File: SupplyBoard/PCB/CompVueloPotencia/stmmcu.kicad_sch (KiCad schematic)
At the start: 20 parts, among them J2 USB_B_Micro, J3 Conn_01x04, SW2 RESET, SW3 SW_SPDT, U4 STM32F103CBT6, Y1 16Mhz

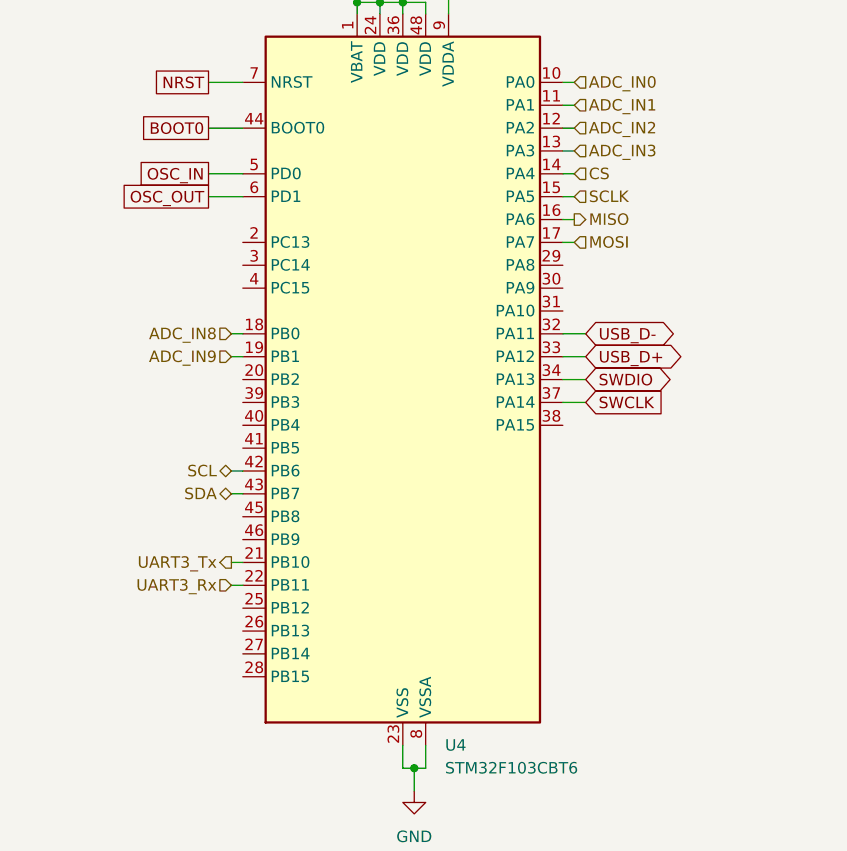
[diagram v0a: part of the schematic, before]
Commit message: Supply board - Update the current measurement
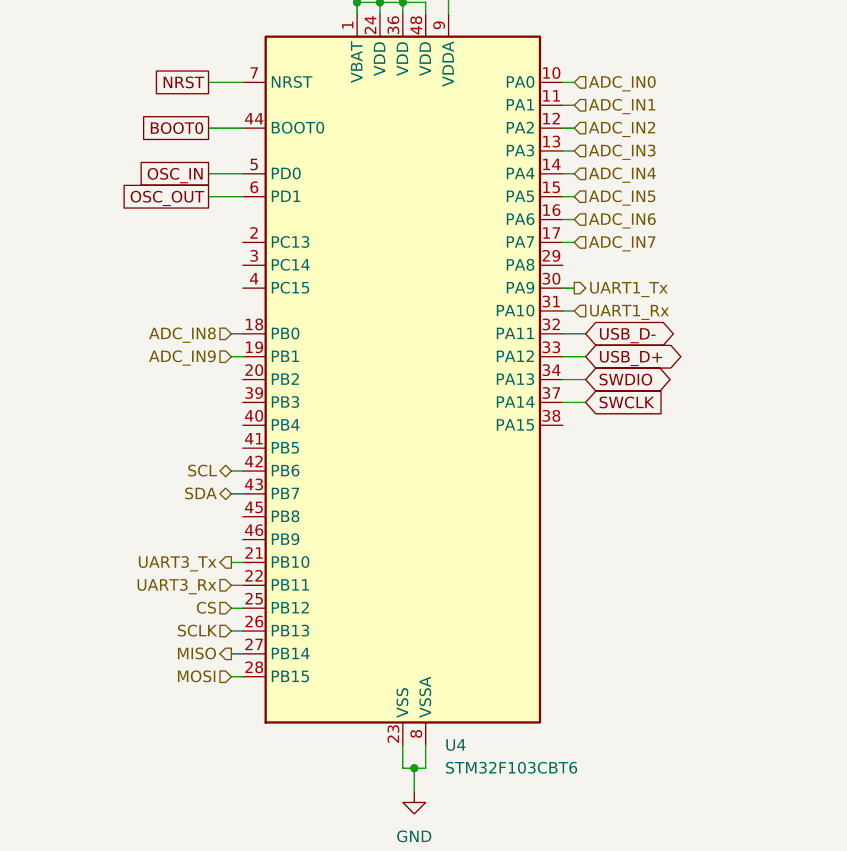
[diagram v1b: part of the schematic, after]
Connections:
- net CS: now also U4.25 (PB12); no longer U4.14 (PA4)
- net MISO: now also U4.27 (PB14); no longer U4.16 (PA6)
- net MOSI: now also U4.28 (PB15); no longer U4.17 (PA7)
- net SCLK: now also U4.26 (PB13); no longer U4.15 (PA5)
- net UART1_Tx: now reaches U4.30 (PA9)
- net UART1_Rx: now reaches U4.31 (PA10)
- new net ADC_IN4: U4.14 (PA4)
- new net ADC_IN5: U4.15 (PA5)
- new net ADC_IN6: U4.16 (PA6)
- new net ADC_IN7: U4.17 (PA7)
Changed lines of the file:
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@@
+	(wire
+		(pts
+			(xy 119.38 124.46) (xy 120.65 124.46)
+		)
+		(stroke
+			(width 0)
+			(type default)
+		)
+	)
 	(wire
 		(pts
@@
 		(pts
 			(xy 31.75 64.77) (xy 35.56 64.77)
+		)
+		(stroke
+			(width 0)
+			(type default)
+		)
+	)
+	(wire
+		(pts
+			(xy 119.38 127) (xy 120.65 127)
 		)
 		(stroke
@@
 	(wire
 		(pts
-			(xy 157.48 76.2) (xy 156.21 76.2)
-		)
-		(stroke
-			(width 0)
-			(type default)
-		)
-	)
-	(wire
-		(pts
 			(xy 138.43 54.61) (xy 135.89 54.61)
 		)
@@
 	(wire
 		(pts
+			(xy 45.72 123.19) (xy 45.72 119.38)
+		)
+		(stroke
+			(width 0)
+			(type default)
+		)
+	)
+	(wire
+		(pts
+			(xy 138.43 139.7) (xy 139.7 139.7)
+		)
+		(stroke
+			(width 0)
+			(type default)
+		)
+	)
+	(wire
+		(pts
+			(xy 233.68 48.26) (xy 233.68 45.72)
+		)
+		(stroke
+			(width 0)
+			(type default)
+		)
+	)
+	(wire
+		(pts
+			(xy 240.03 132.08) (xy 242.57 132.08)
+		)
+		(stroke
+			(width 0)
+			(type default)
+		)
+	)
+	(wire
+		(pts
+			(xy 240.03 129.54) (xy 242.57 129.54)
+		)
+		(stroke
+			(width 0)
+			(type default)
+		)
+	)
+	(wire
+		(pts
+			(xy 240.03 38.1) (xy 246.38 38.1)
+		)
+		(stroke
+			(width 0)
+			(type default)
+		)
+	)
+	(wire
+		(pts
+			(xy 35.56 111.76) (xy 35.56 110.49)
+		)
+		(stroke
+			(width 0)
+			(type default)
+		)
+	)
+	(wire
+		(pts
+			(xy 21.59 168.91) (xy 21.59 171.45)
+		)
+		(stroke
+			(width 0)
+			(type default)
+		)
+	)
+	(wire
+		(pts
+			(xy 157.48 88.9) (xy 156.21 88.9)
+		)
+		(stroke
+			(width 0)
+			(type default)
+		)
+	)
+	(wire
+		(pts
+			(xy 157.48 76.2) (xy 156.21 76.2)
+		)
+		(stroke
+			(width 0)
+			(type default)
+		)
+	)
+	(wire
+		(pts
 			(xy 157.48 81.28) (xy 156.21 81.28)
 		)
@@
 	(wire
 		(pts
-			(xy 45.72 123.19) (xy 45.72 119.38)
-		)
-		(stroke
-			(width 0)
-			(type default)
-		)
-	)
-	(wire
-		(pts
-			(xy 138.43 139.7) (xy 139.7 139.7)
-		)
-		(stroke
-			(width 0)
-			(type default)
-		)
-	)
-	(wire
-		(pts
-			(xy 233.68 48.26) (xy 233.68 45.72)
-		)
-		(stroke
-			(width 0)
-			(type default)
-		)
-	)
-	(wire
-		(pts
-			(xy 240.03 132.08) (xy 242.57 132.08)
-		)
-		(stroke
-			(width 0)
-			(type default)
-		)
-	)
-	(wire
-		(pts
-			(xy 240.03 129.54) (xy 242.57 129.54)
-		)
-		(stroke
-			(width 0)
-			(type default)
-		)
-	)
-	(wire
-		(pts
-			(xy 240.03 38.1) (xy 246.38 38.1)
-		)
-		(stroke
-			(width 0)
-			(type default)
-		)
-	)
-	(wire
-		(pts
-			(xy 35.56 111.76) (xy 35.56 110.49)
-		)
-		(stroke
-			(width 0)
-			(type default)
-		)
-	)
-	(wire
-		(pts
-			(xy 21.59 168.91) (xy 21.59 171.45)
-		)
-		(stroke
-			(width 0)
-			(type default)
-		)
-	)
-	(wire
-		(pts
 			(xy 45.72 115.57) (xy 45.72 119.38)
 		)
@@
 	(wire
 		(pts
+			(xy 157.48 78.74) (xy 156.21 78.74)
+		)
+		(stroke
+			(width 0)
+			(type default)
+		)
+	)
+	(wire
+		(pts
+			(xy 119.38 121.92) (xy 120.65 121.92)
+		)
+		(stroke
+			(width 0)
+			(type default)
+		)
+	)
+	(wire
+		(pts
 			(xy 35.56 110.49) (xy 41.91 110.49)
 		)
@@
 		(pts
 			(xy 133.35 54.61) (xy 133.35 55.88)
+		)
+		(stroke
+			(width 0)
+			(type default)
+		)
+	)
+	(wire
+		(pts
+			(xy 157.48 86.36) (xy 156.21 86.36)
 		)
 		(stroke
@@
 	(wire
 		(pts
+			(xy 157.48 73.66) (xy 156.21 73.66)
+		)
+		(stroke
+			(width 0)
+			(type default)
+		)
+	)
+	(wire
+		(pts
 			(xy 231.14 93.98) (xy 233.68 93.98)
 		)
@@
 	(wire
 		(pts
+			(xy 119.38 129.54) (xy 120.65 129.54)
+		)
+		(stroke
+			(width 0)
+			(type default)
+		)
+	)
+	(wire
+		(pts
 			(xy 119.38 93.98) (xy 120.65 93.98)
 		)
@@
 	(wire
 		(pts
-			(xy 157.48 73.66) (xy 156.21 73.66)
-		)
-		(stroke
-			(width 0)
-			(type default)
-		)
-	)
-	(wire
-		(pts
 			(xy 157.48 71.12) (xy 156.21 71.12)
 		)
@@
 		(pts
 			(xy 49.53 110.49) (xy 54.61 110.49)
-		)
-		(stroke
-			(width 0)
-			(type default)
-		)
-	)
-	(wire
-		(pts
-			(xy 157.48 78.74) (xy 156.21 78.74)
 		)
 		(stroke
@@
 		)
 	)
-	(hierarchical_label "MOSI"
+	(hierarchical_label "CS"
 		(shape input)
-		(at 157.48 81.28 0)
+		(at 119.38 121.92 180)
+		(effects
+			(font
+				(size 1.27 1.27)
+			)
+			(justify right)
+		)
+	)
+	(hierarchical_label "ADC_IN4"
+		(shape input)
+		(at 157.48 73.66 0)
 		(effects
 			(font
@@
 		)
 	)
-	(hierarchical_label "SCLK"
-		(shape input)
-		(at 157.48 76.2 0)
-		(effects
-			(font
-				(size 1.27 1.27)
-			)
-			(justify left)
-		)
-	)
 	(hierarchical_label "UART3_Rx"
 		(shape input)
@@
 		)
 	)
+	(hierarchical_label "UART1_Tx"
+		(shape output)
+		(at 157.48 86.36 0)
+		(effects
+			(font
+				(size 1.27 1.27)
+			)
+			(justify left)
+		)
+	)
 	(hierarchical_label "ADC_IN2"
 		(shape input)
@@
 		)
 	)
+	(hierarchical_label "ADC_IN6"
+		(shape input)
+		(at 157.48 78.74 0)
+		(effects
+			(font
+				(size 1.27 1.27)
+			)
+			(justify left)
+		)
+	)
 	(hierarchical_label "ADC_IN3"
 		(shape input)
@@
 		)
 	)
+	(hierarchical_label "MOSI"
+		(shape input)
+		(at 119.38 129.54 180)
+		(effects
+			(font
+				(size 1.27 1.27)
+			)
+			(justify right)
+		)
+	)
+	(hierarchical_label "MISO"
+		(shape output)
+		(at 119.38 127 180)
+		(effects
+			(font
+				(size 1.27 1.27)
+			)
+			(justify right)
+		)
+	)
 	(hierarchical_label "VDD"
 		(shape input)
@@
 		)
 	)
-	(hierarchical_label "CS"
+	(hierarchical_label "ADC_IN7"
 		(shape input)
-		(at 157.48 73.66 0)
+		(at 157.48 81.28 0)
 		(effects
 			(font
@@
 		)
 	)
-	(hierarchical_label "MISO"
-		(shape output)
-		(at 157.48 78.74 0)
+	(hierarchical_label "ADC_IN5"
+		(shape input)
+		(at 157.48 76.2 0)
 		(effects
 			(font
@@
 		)
 	)
+	(hierarchical_label "SCLK"
+		(shape input)
+		(at 119.38 124.46 180)
+		(effects
+			(font
+				(size 1.27 1.27)
+			)
+			(justify right)
+		)
+	)
 	(hierarchical_label "ADC_IN1"
 		(shape input)
@@
 		)
 	)
+	(hierarchical_label "UART1_Rx"
+		(shape input)
+		(at 157.48 88.9 0)
+		(effects
+			(font
+				(size 1.27 1.27)
+			)
+			(justify left)
+		)
+	)

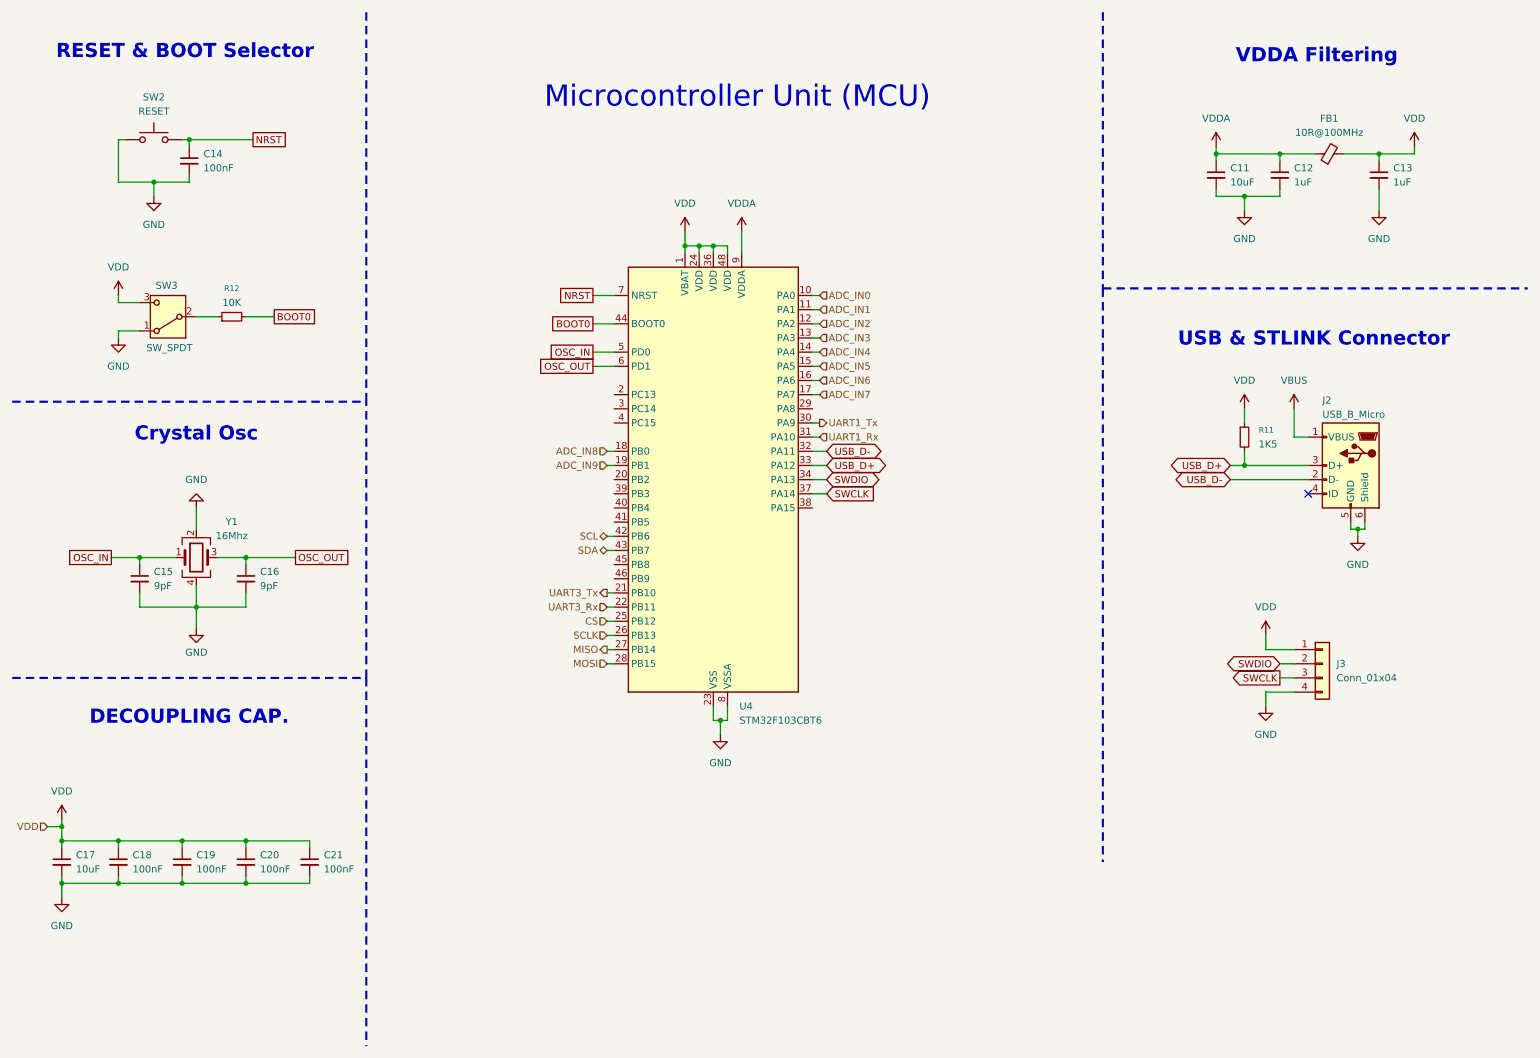
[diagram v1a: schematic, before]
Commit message: SupplyBoard - finish current sense
Finish the Current Sensor Circuit and add more 3.3V out, i change de microcontroles to a mcu that have the exact GPIO's
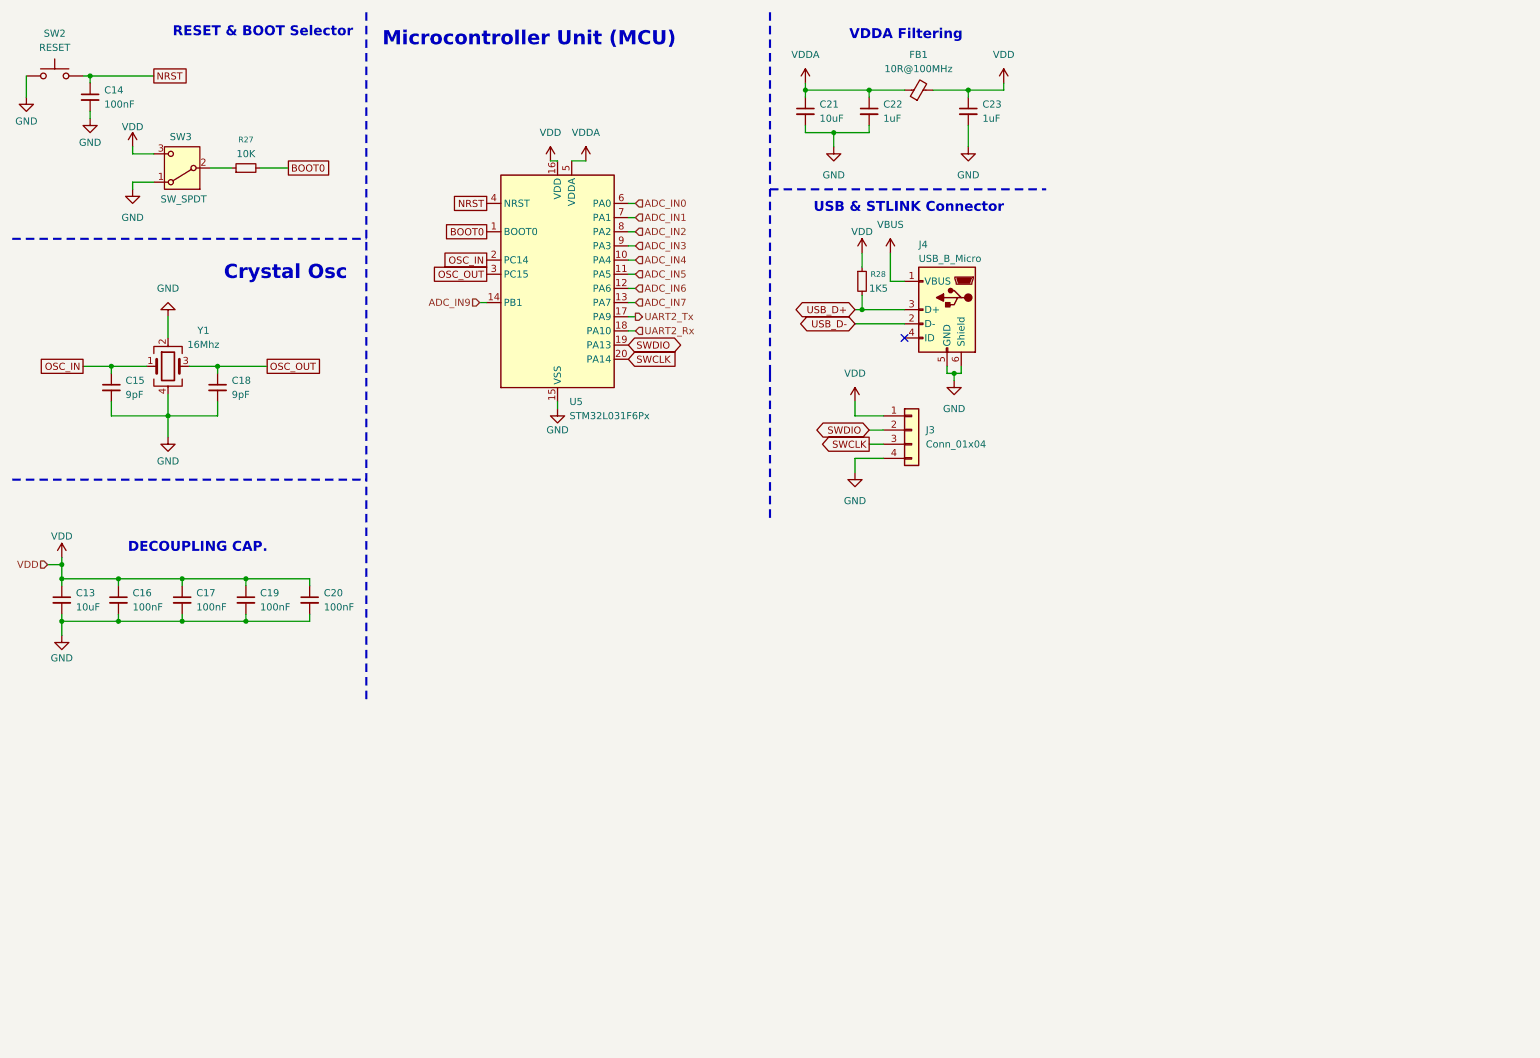
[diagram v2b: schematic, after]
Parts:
- removed U4: STM32F103CBT6, Package_QFP:LQFP-48_7x7mm_P0.5mm, symbol MCU_ST_STM32F1:STM32F103CBTx
- added U5: STM32L031F6Px, Package_SO:TSSOP-20_4.4x6.5mm_P0.65mm, symbol MCU_ST_STM32L0:STM32L031F6Px
- renumbered C17 to C13, C18 to C16, C19 to C17, C16 to C18, C20 to C19, C21 to C20, C11 to C21, C12 to C22, C13 to C23, J2 to J4, R12 to R27, R11 to R28
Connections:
- net ADC_IN0: now also U5.6 (PA0)
- net ADC_IN1: now also U5.7 (PA1)
- net ADC_IN2: now also U5.8 (PA2)
- net ADC_IN3: now also U5.9 (PA3)
- net ADC_IN4: now also U5.10 (PA4)
- net ADC_IN5: now also U5.11 (PA5)
- net ADC_IN6: now also U5.12 (PA6)
- net ADC_IN7: now also U5.13 (PA7)
- net ADC_IN9: now also U5.14 (PB1)
- net BOOT0: now also U5.1 (BOOT0)
- net GND: now also U5.15 (VSS)
- net NRST: now also U5.4 (NRST)
- net OSC_IN: now also U5.2 (PC14)
- net OSC_OUT: now also U5.3 (PC15)
- net SWCLK: now also U5.20 (PA14)
- net SWDIO: now also U5.19 (PA13)
- net VDD: now also U5.16 (VDD)
- net VDDA: now also U5.5 (VDDA)
- new net UART2_Rx: U5.18 (PA10)
- new net UART2_Tx: U5.17 (PA9)
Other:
- moved on the sheet: C13, C14, C15, C16, C17, C18, C19, C20, C21, C22, C23, FB1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

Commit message: SupplyBoard - update layout
schematic completed and PCB layout started; only the routing of the traces remains to be done
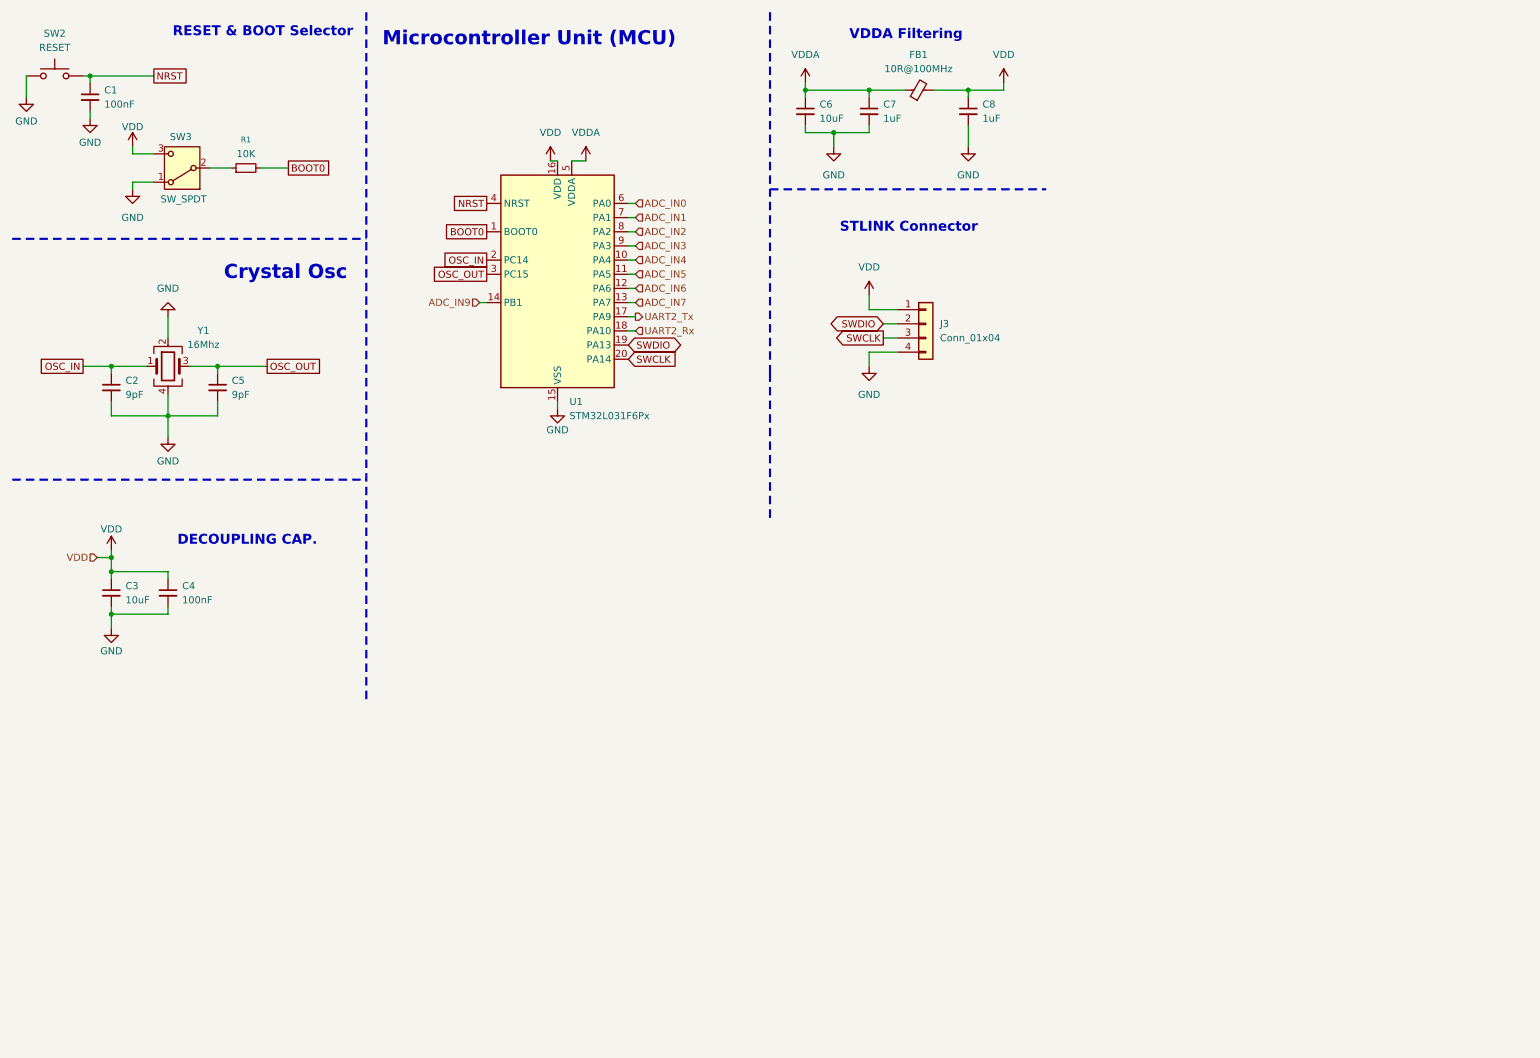
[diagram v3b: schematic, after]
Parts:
- removed C17, C19, C20: 100nF, symbol Device:C_Small
- removed J4: USB_B_Micro, symbol Connector:USB_B_Micro
- removed R28: 1K5, symbol Device:R_Small
- C1: renamed from C14; footprint (none) -> Capacitor_SMD:C_0805_2012Metric_Pad1.18x1.45mm_HandSolder
- C2: renamed from C15; footprint (none) -> Capacitor_SMD:C_0805_2012Metric_Pad1.18x1.45mm_HandSolder
- C3: renamed from C13; footprint (none) -> Capacitor_SMD:C_0805_2012Metric_Pad1.18x1.45mm_HandSolder
- C4: renamed from C16; footprint (none) -> Capacitor_SMD:C_0805_2012Metric_Pad1.18x1.45mm_HandSolder
- C5: renamed from C18; footprint (none) -> Capacitor_SMD:C_0805_2012Metric_Pad1.18x1.45mm_HandSolder
- C6: renamed from C21; footprint (none) -> Capacitor_SMD:C_0805_2012Metric_Pad1.18x1.45mm_HandSolder
- C7: renamed from C22; footprint (none) -> Capacitor_SMD:C_0805_2012Metric_Pad1.18x1.45mm_HandSolder
- C8: renamed from C23; footprint (none) -> Capacitor_SMD:C_0805_2012Metric_Pad1.18x1.45mm_HandSolder
- FB1: footprint (none) -> Inductor_SMD:L_0402_1005Metric_Pad0.77x0.64mm_HandSolder
- J3: footprint (none) -> Connector_PinHeader_2.54mm:PinHeader_1x04_P2.54mm_Vertical
- R1: renamed from R27; footprint (none) -> Resistor_SMD:R_0805_2012Metric_Pad1.20x1.40mm_HandSolder
- SW2: footprint (none) -> Button_Switch_SMD:SW_Push_1P1T_XKB_TS-1187A
- SW3: footprint (none) -> Connector_PinHeader_2.54mm:PinHeader_1x03_P2.54mm_Vertical
- Y1: footprint (none) -> Crystal:Crystal_SMD_0603-4Pin_6.0x3.5mm_HandSoldering
- renumbered U5 to U1
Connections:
- no-connect marks 1 -> 0
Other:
- note added: "STLINK Connector"
- note removed: "USB & STLINK Connector"
- moved on the sheet: C3, C4, J3
